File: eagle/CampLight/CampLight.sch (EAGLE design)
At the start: 27 parts, among them U1 ATMEGA328P_PDIP

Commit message: Latest Camplight work
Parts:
- removed IC1: (no value), SparkFun-PowerIC:V_REG_78XX-TO-220
- removed U$1: DIODE-ZENERPTH, SparkFun-DiscreteSemi:DIODE-ZENERPTH
- added D1: (no value), SparkFun-DiscreteSemi:DIODEPTH
- added LED7: (no value), SparkFun-LED:LED3MM
- added R8: (no value), SparkFun-Resistors:RESISTORAXIAL-0.3
- added VREG: (no value), v-reg:78LXX
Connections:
- new net N$19: LED7.C, R8.2
- new net N$20: LED7.A, U1.PD4(XCK/T0)
- net 5V: now also VREG.OUT; no longer IC1.OUT
- net GND: now also R8.1, VREG.GND; no longer IC1.GND
- net N$1: now also D1.C, VREG.IN; no longer IC1.IN, U$1.C
- net N$5: now also D1.A; no longer U$1.A
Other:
- note added: "Battery Test"
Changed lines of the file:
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@@
 <part name="U1" library="SparkFun-DigitalIC" deviceset="ATMEGA328P_PDIP" device=""/>
 <part name="Y1" library="SparkFun-FreqCtrl" deviceset="RESONATOR" device="PTH"/>
-<part name="IC1" library="SparkFun-PowerIC" deviceset="V_REG_78XX" device="-TO-220"/>
+<part name="VREG" library="v-reg" deviceset="78LXX" device=""/>
 <part name="C1" library="SparkFun-Passives" deviceset="CAP_POL" device="PTH2"/>
 <part name="C2" library="SparkFun-Passives" deviceset="CAP_POL" device="PTH2"/>
@@
 <part name="R5" library="SparkFun-Resistors" deviceset="RESISTOR" device="AXIAL-0.3"/>
 <part name="R6" library="SparkFun-Resistors" deviceset="RESISTOR" device="AXIAL-0.3"/>
-<part name="U$1" library="SparkFun-DiscreteSemi" deviceset="DIODE-ZENER" device="PTH"/>
 <part name="Q1" library="SparkFun-DiscreteSemi" deviceset="TRANSISTOR_NPN" device="TO-92-AMMO"/>
 <part name="POT" library="SparkFun-Passives" deviceset="JUMPER-3" device="PTH"/>
@@
 <part name="C4" library="SparkFun-Passives" deviceset="CAP" device="PTH"/>
 <part name="R7" library="SparkFun-Passives" deviceset="RESISTOR" device="PTH-1/4W"/>
+<part name="LED7" library="SparkFun-LED" deviceset="LED" device="3MM"/>
+<part name="R8" library="SparkFun-Resistors" deviceset="RESISTOR" device="AXIAL-0.3"/>
+<part name="GND6" library="SparkFun-Aesthetics" deviceset="GND" device=""/>
+<part name="SUPPLY5" library="SparkFun-Aesthetics" deviceset="5V" device=""/>
+<part name="D1" library="SparkFun-DiscreteSemi" deviceset="DIODE" device="PTH"/>
 </parts>
 <sheets>
@@
 <plain>
 <text x="241.3" y="7.62" size="3.81" layer="91">1</text>
+<text x="93.98" y="172.72" size="1.778" layer="91">Battery
+Test</text>
 </plain>
 <instances>
@@
 <instance part="U1" gate="G$1" x="63.5" y="119.38"/>
 <instance part="Y1" gate="G$1" x="38.1" y="116.84" rot="R270"/>
-<instance part="IC1" gate="G$1" x="198.12" y="109.22"/>
+<instance part="VREG" gate="1" x="198.12" y="109.22"/>
 <instance part="C1" gate="G$1" x="215.9" y="101.6"/>
 <instance part="C2" gate="G$1" x="180.34" y="101.6"/>
@@
 <instance part="R5" gate="G$1" x="132.08" y="91.44" rot="R90"/>
 <instance part="R6" gate="G$1" x="132.08" y="71.12" rot="R90"/>
-<instance part="U$1" gate="G$1" x="208.28" y="121.92" rot="R180"/>
 <instance part="Q1" gate="G$1" x="114.3" y="63.5"/>
 <instance part="POT" gate="G$1" x="200.66" y="134.62" rot="R90"/>
@@
 <instance part="C4" gate="G$1" x="35.56" y="152.4"/>
 <instance part="R7" gate="G$1" x="109.22" y="88.9" rot="R90"/>
+<instance part="LED7" gate="G$1" x="104.14" y="73.66"/>
+<instance part="R8" gate="G$1" x="104.14" y="60.96" rot="R90"/>
+<instance part="GND6" gate="1" x="104.14" y="50.8"/>
+<instance part="SUPPLY5" gate="G$1" x="96.52" y="165.1"/>
+<instance part="D1" gate="G$1" x="210.82" y="124.46" rot="R180"/>
 </instances>
 <busses>
@@
 </segment>
 <segment>
-<pinref part="IC1" gate="G$1" pin="OUT"/>
+<pinref part="VREG" gate="1" pin="OUT"/>
 <pinref part="C1" gate="G$1" pin="+"/>
 <wire x1="205.74" y1="109.22" x2="215.9" y2="109.22" width="0.1524" layer="91"/>
@@
 <wire x1="149.86" y1="83.82" x2="139.7" y2="83.82" width="0.1524" layer="91"/>
 </segment>
+<segment>
+<pinref part="SUPPLY5" gate="G$1" pin="5V"/>
+<wire x1="96.52" y1="165.1" x2="96.52" y2="142.24" width="0.1524" layer="91"/>
+<wire x1="96.52" y1="142.24" x2="86.36" y2="142.24" width="0.1524" layer="91"/>
+</segment>
 </net>
 <net name="GND" class="0">
@@
 <wire x1="215.9" y1="91.44" x2="215.9" y2="96.52" width="0.1524" layer="91"/>
 <junction x="198.12" y="91.44"/>
-<pinref part="IC1" gate="G$1" pin="GND"/>
+<pinref part="VREG" gate="1" pin="GND"/>
 <wire x1="198.12" y1="101.6" x2="198.12" y2="91.44" width="0.1524" layer="91"/>
 <pinref part="GND2" gate="1" pin="GND"/>
@@
 <wire x1="116.84" y1="58.42" x2="116.84" y2="45.72" width="0.1524" layer="91"/>
 </segment>
+<segment>
+<pinref part="R8" gate="G$1" pin="1"/>
+<pinref part="GND6" gate="1" pin="GND"/>
+<wire x1="104.14" y1="55.88" x2="104.14" y2="53.34" width="0.1524" layer="91"/>
+</segment>
 </net>
 <net name="N$1" class="0">
 <segment>
-<pinref part="IC1" gate="G$1" pin="IN"/>
+<pinref part="VREG" gate="1" pin="IN"/>
 <pinref part="C2" gate="G$1" pin="+"/>
 <wire x1="190.5" y1="109.22" x2="180.34" y2="109.22" width="0.1524" layer="91"/>
 <wire x1="180.34" y1="109.22" x2="180.34" y2="104.14" width="0.1524" layer="91"/>
 <junction x="180.34" y="109.22"/>
-<pinref part="U$1" gate="G$1" pin="C"/>
-<wire x1="205.74" y1="121.92" x2="180.34" y2="121.92" width="0.1524" layer="91"/>
-<wire x1="180.34" y1="121.92" x2="180.34" y2="109.22" width="0.1524" layer="91"/>
+<wire x1="180.34" y1="124.46" x2="180.34" y2="109.22" width="0.1524" layer="91"/>
+<pinref part="D1" gate="G$1" pin="C"/>
+<wire x1="180.34" y1="124.46" x2="208.28" y2="124.46" width="0.1524" layer="91"/>
 </segment>
 </net>
@@
 <segment>
 <pinref part="SWITCH" gate="A" pin="2"/>
-<pinref part="U$1" gate="G$1" pin="A"/>
-<wire x1="223.52" y1="119.38" x2="223.52" y2="121.92" width="0.1524" layer="91"/>
-<wire x1="223.52" y1="121.92" x2="210.82" y2="121.92" width="0.1524" layer="91"/>
+<pinref part="D1" gate="G$1" pin="A"/>
+<wire x1="223.52" y1="119.38" x2="223.52" y2="124.46" width="0.1524" layer="91"/>
+<wire x1="223.52" y1="124.46" x2="213.36" y2="124.46" width="0.1524" layer="91"/>
 </segment>
 </net>
@@
 </segment>
 </net>
+<net name="N$19" class="0">
+<segment>
+<pinref part="LED7" gate="G$1" pin="C"/>
+<pinref part="R8" gate="G$1" pin="2"/>
+<wire x1="104.14" y1="68.58" x2="104.14" y2="66.04" width="0.1524" layer="91"/>
+</segment>
+</net>
+<net name="N$20" class="0">
+<segment>
+<pinref part="LED7" gate="G$1" pin="A"/>
+<pinref part="U1" gate="G$1" pin="PD4(XCK/T0)"/>
+<wire x1="104.14" y1="76.2" x2="104.14" y2="111.76" width="0.1524" layer="91"/>
+<wire x1="104.14" y1="111.76" x2="88.9" y2="111.76" width="0.1524" layer="91"/>
+</segment>
+</net>
 </nets>
 </sheet>
@@
 </schematic>
 </drawing>
+<compatibility>
+<note version="6.3" minversion="6.2.2" severity="warning">
+Since Version 6.2.2 text objects can contain more than one line,
+which will not be processed correctly with this version.
+</note>
+</compatibility>
 </eagle>

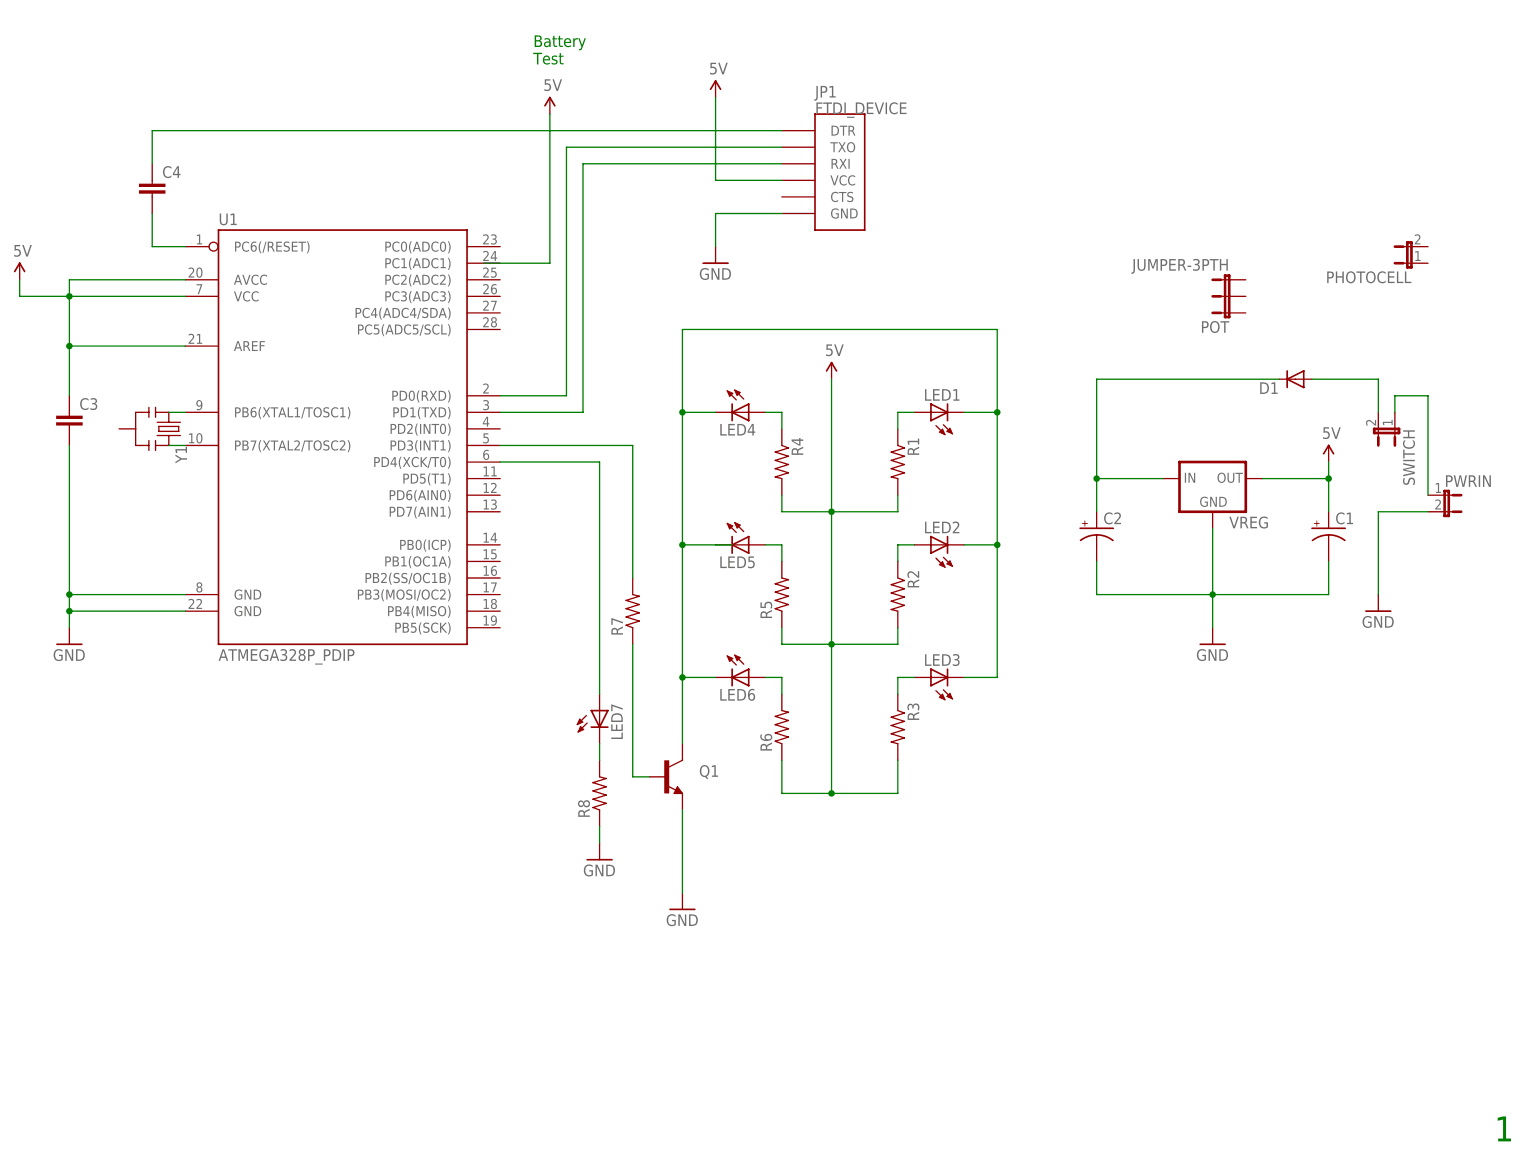
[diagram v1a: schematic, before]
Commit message: Update eagle files with touch switch
This is a final release candidate. I have sent this board to Osh Park (oshpark.com) for fabrication.
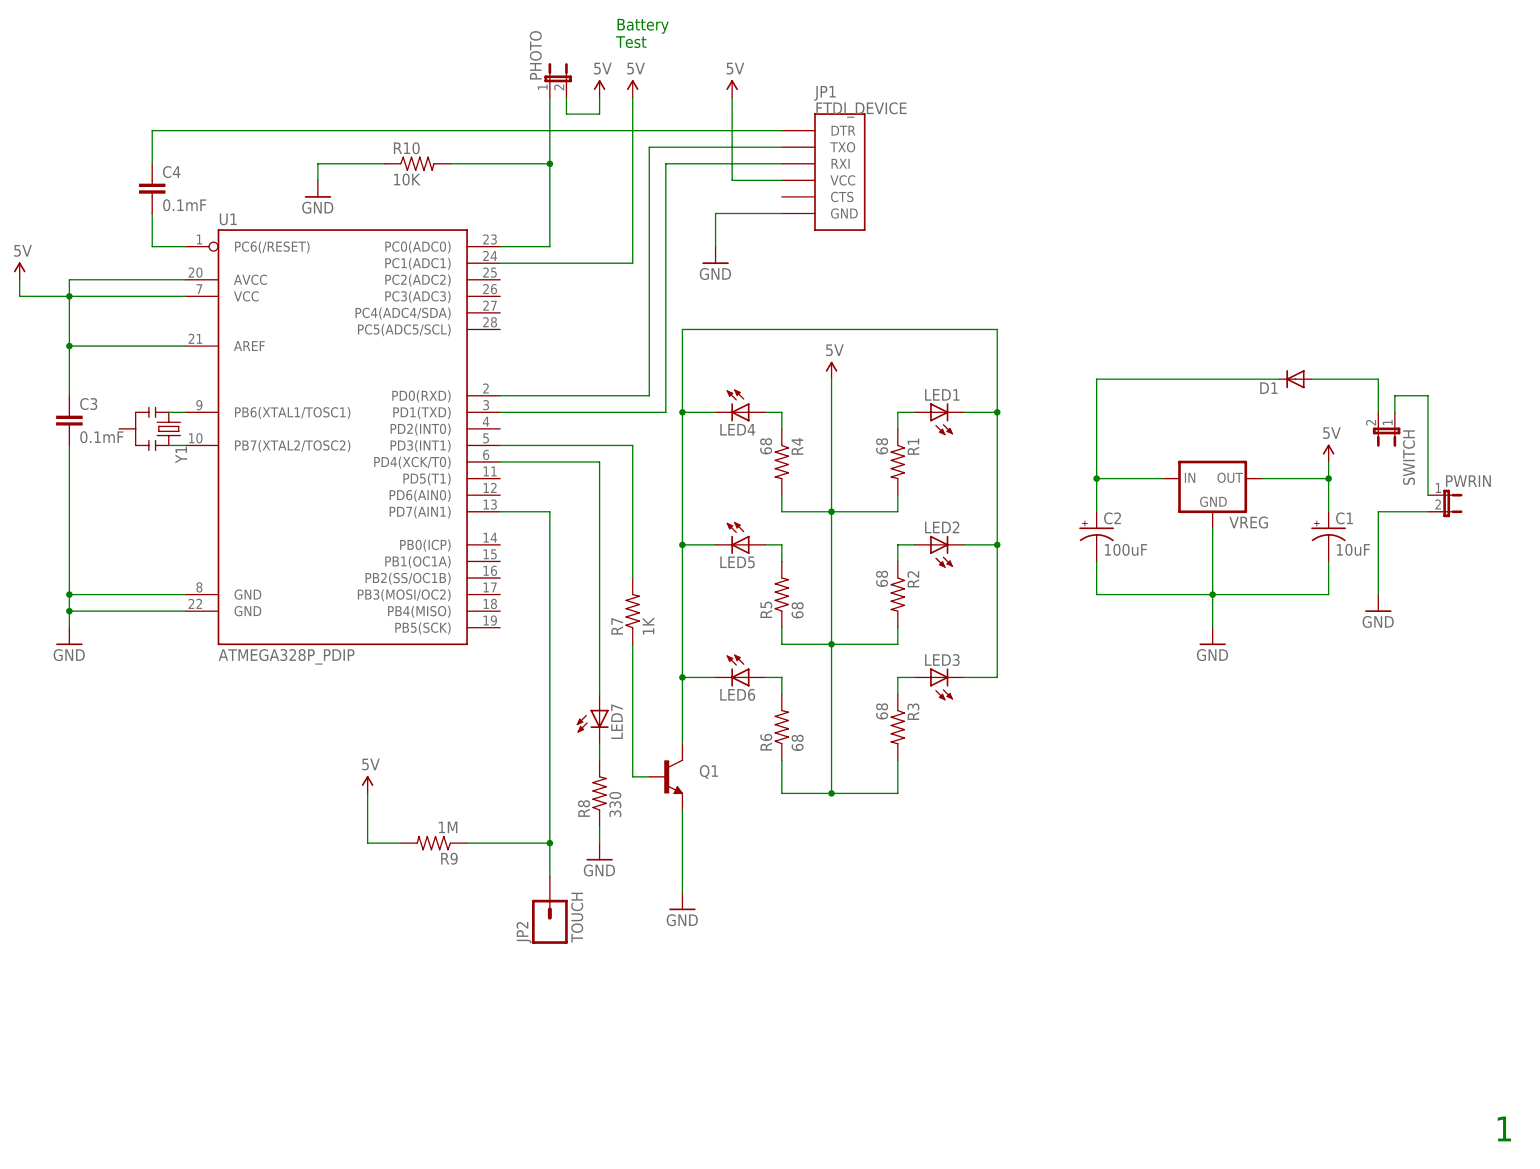
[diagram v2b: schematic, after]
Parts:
- removed PHOTOCELL: (no value), SparkFun-Passives:JUMPER-2PTH_LOCK
- removed POT: JUMPER-3PTH, SparkFun-Passives:JUMPER-3PTH
- added JP2: TOUCH, SparkFun-Connectors:M01PTH
- added PHOTO: (no value), SparkFun-Passives:JUMPER-2PTH_LOCK
- added R10: 10K, SparkFun-Resistors:RESISTORAXIAL-0.3
- added R9: 1M, SparkFun-Passives:RESISTORPTH-1/4W
- C1: value (none) -> 10uF
- C2: value (none) -> 100uF
- C3, C4: value (none) -> 0.1mF
- R1, R2, R3, R4, R5, R6: value (none) -> 68
- R7: value (none) -> 1K
- R8: value (none) -> 330
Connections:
- new net N$21: JP2.1, R9.1, U1.PD7(AIN1)
- new net N$24: PHOTO.1, R10.2, U1.PC0(ADC0)
- net 5V: now also PHOTO.2, R9.2, U1.PC1(ADC1)
- net GND: now also R10.1
- net N$7: now also LED3.C

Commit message: Update camplight eagle files * Add pull up resistor to reset pin * reverse R & T on programming header
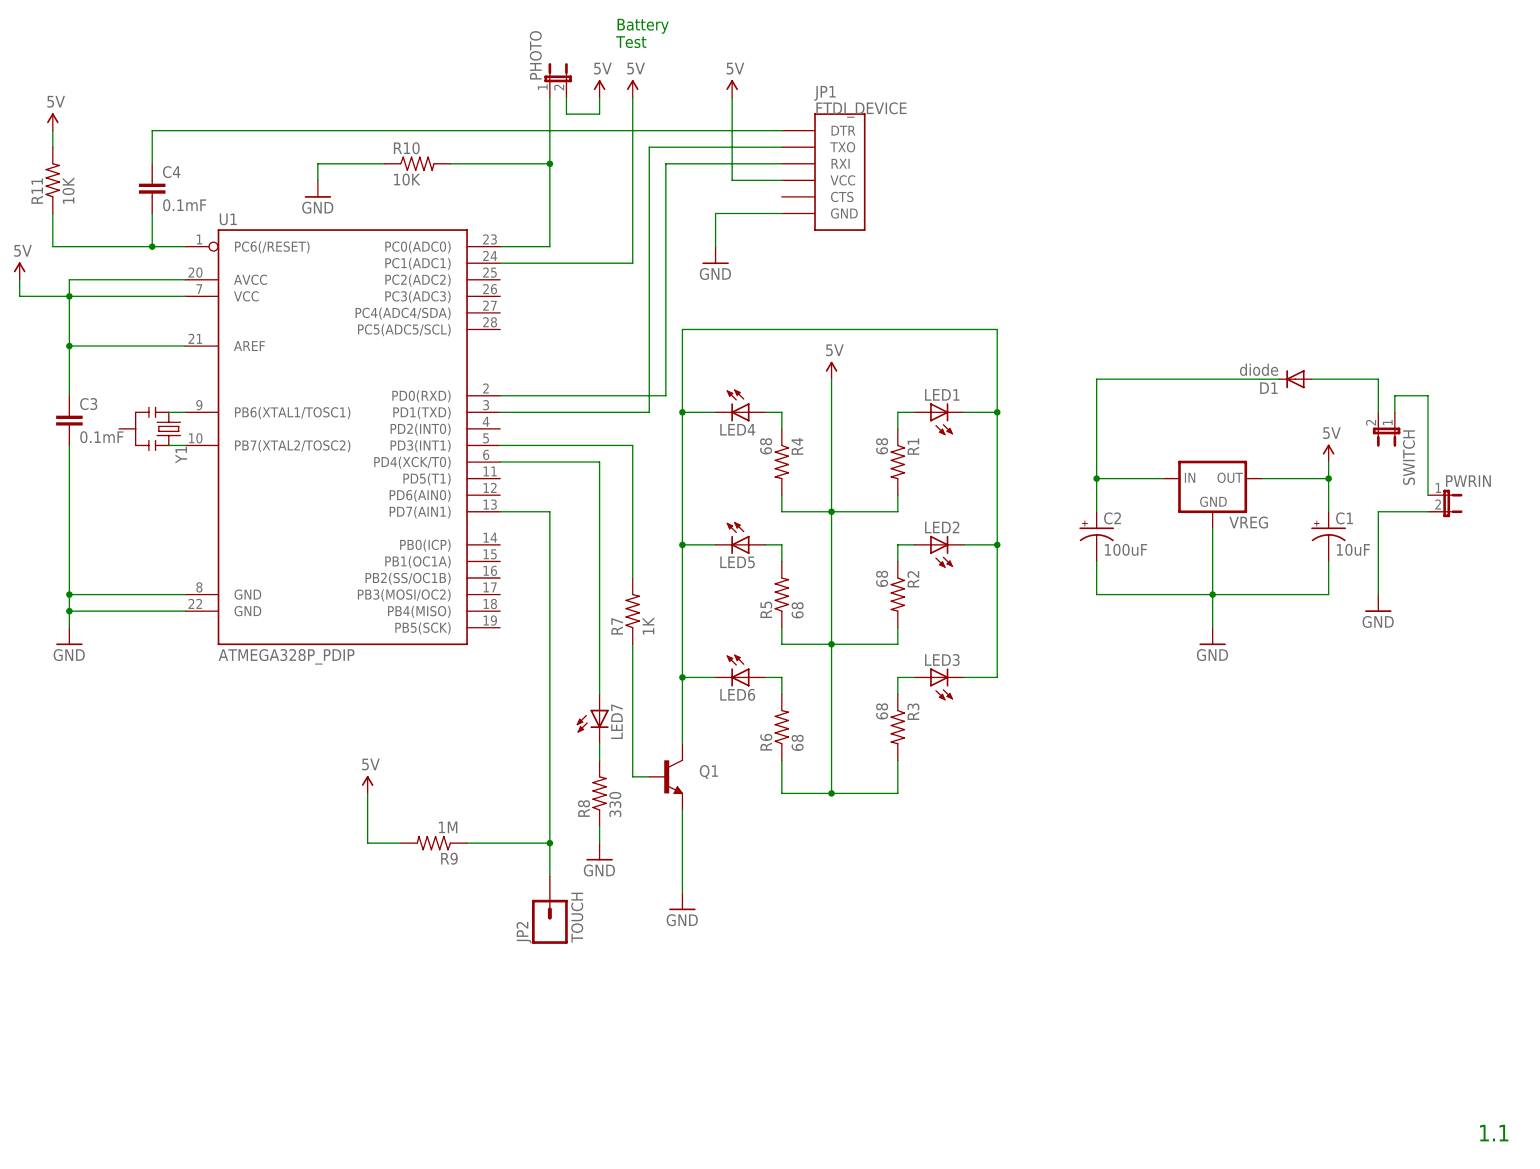
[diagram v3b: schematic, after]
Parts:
- added R11: 10K, SparkFun-Resistors:RESISTORAXIAL-0.3
- D1: value (none) -> diode
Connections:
- net 5V: now also R11.2
- net N$12: now also U1.PD0(RXD); no longer U1.PD1(TXD)
- net N$15: now also U1.PD1(TXD); no longer U1.PD0(RXD)
- net N$16: now also R11.1
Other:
- note added: "1.1"
- note removed: "1"
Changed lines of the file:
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@@
 </classes>
 <parts>
-<part name="CAMPLIGHT" library="frames" deviceset="LETTER_L" device=""/>
+<part name="CAMPLIGHT" library="frames" deviceset="LETTER_L" device="" value="sheet"/>
 <part name="U1" library="SparkFun-DigitalIC" deviceset="ATMEGA328P_PDIP" device=""/>
 <part name="Y1" library="SparkFun-FreqCtrl" deviceset="RESONATOR" device="PTH"/>
@@
 <part name="GND6" library="SparkFun-Aesthetics" deviceset="GND" device=""/>
 <part name="SUPPLY5" library="SparkFun-Aesthetics" deviceset="5V" device=""/>
-<part name="D1" library="SparkFun-DiscreteSemi" deviceset="DIODE" device="PTH"/>
+<part name="D1" library="SparkFun-DiscreteSemi" deviceset="DIODE" device="PTH" value="diode"/>
 <part name="R9" library="SparkFun-Passives" deviceset="RESISTOR" device="PTH-1/4W" value="1M"/>
 <part name="SUPPLY6" library="SparkFun-Aesthetics" deviceset="5V" device=""/>
@@
 <part name="SUPPLY7" library="SparkFun-Aesthetics" deviceset="5V" device=""/>
 <part name="SUPPLY8" library="SparkFun-Aesthetics" deviceset="5V" device=""/>
+<part name="R11" library="SparkFun-Resistors" deviceset="RESISTOR" device="AXIAL-0.3" value="10K"/>
+<part name="SUPPLY3" library="SparkFun-Aesthetics" deviceset="5V" device=""/>
 </parts>
 <sheets>
 <sheet>
 <plain>
-<text x="241.3" y="7.62" size="3.81" layer="91">1</text>
 <text x="106.68" y="175.26" size="1.778" layer="91">Battery
 Test</text>
+<text x="238.76" y="7.62" size="2.54" layer="91">1.1</text>
 </plain>
 <instances>
@@
 <instance part="SUPPLY7" gate="G$1" x="124.46" y="167.64"/>
 <instance part="SUPPLY8" gate="G$1" x="104.14" y="167.64"/>
+<instance part="R11" gate="G$1" x="20.32" y="154.94" rot="R90"/>
+<instance part="SUPPLY3" gate="G$1" x="20.32" y="162.56"/>
 </instances>
 <busses>
@@
 <pinref part="SUPPLY7" gate="G$1" pin="5V"/>
 <wire x1="124.46" y1="154.94" x2="124.46" y2="167.64" width="0.1524" layer="91"/>
+</segment>
+<segment>
+<pinref part="R11" gate="G$1" pin="2"/>
+<pinref part="SUPPLY3" gate="G$1" pin="5V"/>
+<wire x1="20.32" y1="160.02" x2="20.32" y2="162.56" width="0.1524" layer="91"/>
 </segment>
 </net>
@@
 <net name="N$12" class="0">
 <segment>
-<pinref part="U1" gate="G$1" pin="PD1(TXD)"/>
-<wire x1="88.9" y1="119.38" x2="114.3" y2="119.38" width="0.1524" layer="91"/>
 <pinref part="JP1" gate="G$1" pin="RXI"/>
-<wire x1="114.3" y1="119.38" x2="114.3" y2="157.48" width="0.1524" layer="91"/>
+<wire x1="114.3" y1="121.92" x2="114.3" y2="157.48" width="0.1524" layer="91"/>
 <wire x1="114.3" y1="157.48" x2="132.08" y2="157.48" width="0.1524" layer="91"/>
+<pinref part="U1" gate="G$1" pin="PD0(RXD)"/>
+<wire x1="88.9" y1="121.92" x2="114.3" y2="121.92" width="0.1524" layer="91"/>
 </segment>
 </net>
@@
 <pinref part="JP1" gate="G$1" pin="TXO"/>
 <wire x1="132.08" y1="160.02" x2="111.76" y2="160.02" width="0.1524" layer="91"/>
-<wire x1="111.76" y1="160.02" x2="111.76" y2="121.92" width="0.1524" layer="91"/>
-<wire x1="111.76" y1="121.92" x2="88.9" y2="121.92" width="0.1524" layer="91"/>
-<pinref part="U1" gate="G$1" pin="PD0(RXD)"/>
+<wire x1="111.76" y1="160.02" x2="111.76" y2="119.38" width="0.1524" layer="91"/>
+<pinref part="U1" gate="G$1" pin="PD1(TXD)"/>
+<wire x1="111.76" y1="119.38" x2="88.9" y2="119.38" width="0.1524" layer="91"/>
 </segment>
 </net>
@@
 <wire x1="35.56" y1="149.86" x2="35.56" y2="144.78" width="0.1524" layer="91"/>
 <wire x1="35.56" y1="144.78" x2="40.64" y2="144.78" width="0.1524" layer="91"/>
+<junction x="35.56" y="144.78"/>
+<pinref part="R11" gate="G$1" pin="1"/>
+<wire x1="35.56" y1="144.78" x2="20.32" y2="144.78" width="0.1524" layer="91"/>
+<wire x1="20.32" y1="144.78" x2="20.32" y2="149.86" width="0.1524" layer="91"/>
 </segment>
 </net>
@@
 </sheet>
 </sheets>
+<errors>
+</errors>
 </schematic>
 </drawing>
